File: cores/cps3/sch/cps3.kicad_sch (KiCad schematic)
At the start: 11 parts, among them CN6 Conn_02x27_Odd_Even, Q15 ZR

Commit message: additional_informaion_clk
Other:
- note added: "4-Pin Power Connector and 50-pin SCSI Data Cable Connector"
- note added: "CDROM Drive is a CR504-KCM 4X SCSI drive manufactured By Panasonic / Matsushita"
- note added: "Security Cartridge Slot"
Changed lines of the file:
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@@
     (effects (font (size 1.27 1.27)) (justify left bottom))
+  )
+  (text " Security Cartridge Slot" (at 71.12 119.38 180)
+    (effects (font (size 1.27 1.27)) (justify right bottom))
   )
   (text "This pin is connected to \npin 2 of CR7 (R0)\n\n" (at 36.83 72.39 90)
@@
     (effects (font (size 1.27 1.27)) (justify left bottom))
   )
+  (text "4-Pin Power Connector \nand 50-pin SCSI Data\nCable Connector"
+    (at 193.04 90.17 0)
+    (effects (font (size 1.27 1.27)) (justify left bottom))
+  )
   (text "P4" (at 185.42 88.9 0)
     (effects (font (size 1.27 1.27)) (justify left bottom))
@@
     (effects (font (size 1.27 1.27)) (justify left bottom))
   )
+  (text "CDROM Drive is a CR504-KCM 4X SCSI\ndrive manufactured By Panasonic \n/ Matsushita"
+    (at 193.04 96.52 0)
+    (effects (font (size 1.27 1.27)) (justify left bottom))
+  )

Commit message: wip_gll2
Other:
- sheet objects ports: added 2GLL2PPU[6..0], ~{RESET[0..3]}; removed 2GLL2PPU0, 2GLL_A[5..0], ~{RESET[4..1]}
- sheet ppu ports: added 2GLL2PPU[6..0]; removed 2GLL2PPU0, 2GLL_A[5..0]
- sheet simms_flash ports: added ~{RESET[0..3]}; removed ~{RESET[4..1]}
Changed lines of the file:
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@@
     (stroke (width 0) (type default) (color 0 0 0 0))
   )
-  (wire (pts (xy 194.31 162.56) (xy 212.09 162.56))
-    (stroke (width 0) (type default) (color 0 0 0 0))
-  )
   (bus (pts (xy 85.09 161.29) (xy 85.09 163.83))
     (stroke (width 0) (type default) (color 0 0 0 0))
@@
     (stroke (width 0) (type default) (color 0 0 0 0))
   )
-  (wire (pts (xy 223.52 26.67) (xy 240.03 26.67))
-    (stroke (width 0) (type default) (color 0 0 0 0))
-  )
   (bus (pts (xy 46.99 158.75) (xy 46.99 156.21))
     (stroke (width 0) (type default) (color 0 0 0 0))
@@
     (effects (font (size 1.27 1.27)) (justify left bottom))
   )
-  (label "2GLL_A[5..0]" (at 295.91 31.75 180)
+  (label "2GLL2PPU[6..0]" (at 295.91 31.75 180)
     (effects (font (size 1.27 1.27)) (justify right bottom))
   )
@@
     (effects (font (size 1.27 1.27)) (justify right bottom))
   )
-  (label "2GLL_A[5..0]" (at 212.09 119.38 180)
+  (label "2GLL2PPU[6..0]" (at 212.09 119.38 180)
     (effects (font (size 1.27 1.27)) (justify right bottom))
   )
@@
     (effects (font (size 1.27 1.27)) (justify left bottom))
   )
-  (label "~{RESET[4..1]}" (at 295.91 34.29 180)
+  (label "~{RESET[0..3]}" (at 295.91 34.29 180)
     (effects (font (size 1.27 1.27)) (justify right bottom))
   )
@@
     (effects (font (size 1.27 1.27)) (justify left bottom))
   )
-  (label "2GLL2PPU0" (at 223.52 26.67 0)
-    (effects (font (size 1.27 1.27)) (justify left bottom))
-  )
   (label "MAIN_A[28..0]" (at 295.91 152.4 180)
     (effects (font (size 1.27 1.27)) (justify right bottom))
@@
     (effects (font (size 1.27 1.27)) (justify left bottom))
   )
-  (label "2GLL2PPU0" (at 212.09 162.56 180)
-    (effects (font (size 1.27 1.27)) (justify right bottom))
-  )
   (label "VCC" (at 77.47 130.81 180)
     (effects (font (size 1.27 1.27)) (justify right bottom))
@@
     (effects (font (size 1.27 1.27)) (justify right bottom))
   )
-  (label "~{RESET[4..1]}" (at 138.43 259.08 0)
+  (label "~{RESET[0..3]}" (at 138.43 259.08 0)
     (effects (font (size 1.27 1.27)) (justify left bottom))
   )
@@
       (effects (font (size 1.27 1.27)) (justify left))
     )
-    (pin "~{RESET[4..1]}" input (at 156.21 259.08 180)
+    (pin "~{RESET[0..3]}" input (at 156.21 259.08 180)
       (effects (font (size 1.27 1.27)) (justify left))
     )
@@
       (effects (font (size 1.27 1.27)) (justify right))
     )
-    (pin "2GLL_A[5..0]" bidirectional (at 278.13 31.75 0)
+    (pin "2GLL2PPU[6..0]" bidirectional (at 278.13 31.75 0)
       (effects (font (size 1.27 1.27)) (justify right))
     )
@@
       (effects (font (size 1.27 1.27)) (justify right))
     )
-    (pin "~{RESET[4..1]}" output (at 278.13 34.29 0)
+    (pin "~{RESET[0..3]}" output (at 278.13 34.29 0)
       (effects (font (size 1.27 1.27)) (justify right))
     )
@@
       (effects (font (size 1.27 1.27)) (justify left))
     )
-    (pin "2GLL2PPU0" bidirectional (at 240.03 26.67 180)
-      (effects (font (size 1.27 1.27)) (justify left))
-    )
     (pin "2GLL2CCU0" bidirectional (at 240.03 29.21 180)
       (effects (font (size 1.27 1.27)) (justify left))
@@
       (effects (font (size 1.27 1.27)) (justify right))
     )
-    (pin "2GLL_A[5..0]" bidirectional (at 194.31 119.38 0)
+    (pin "2GLL2PPU[6..0]" bidirectional (at 194.31 119.38 0)
       (effects (font (size 1.27 1.27)) (justify right))
     )
@@
       (effects (font (size 1.27 1.27)) (justify right))
     )
-    (pin "2GLL2PPU0" bidirectional (at 194.31 162.56 0)
-      (effects (font (size 1.27 1.27)) (justify right))
-    )

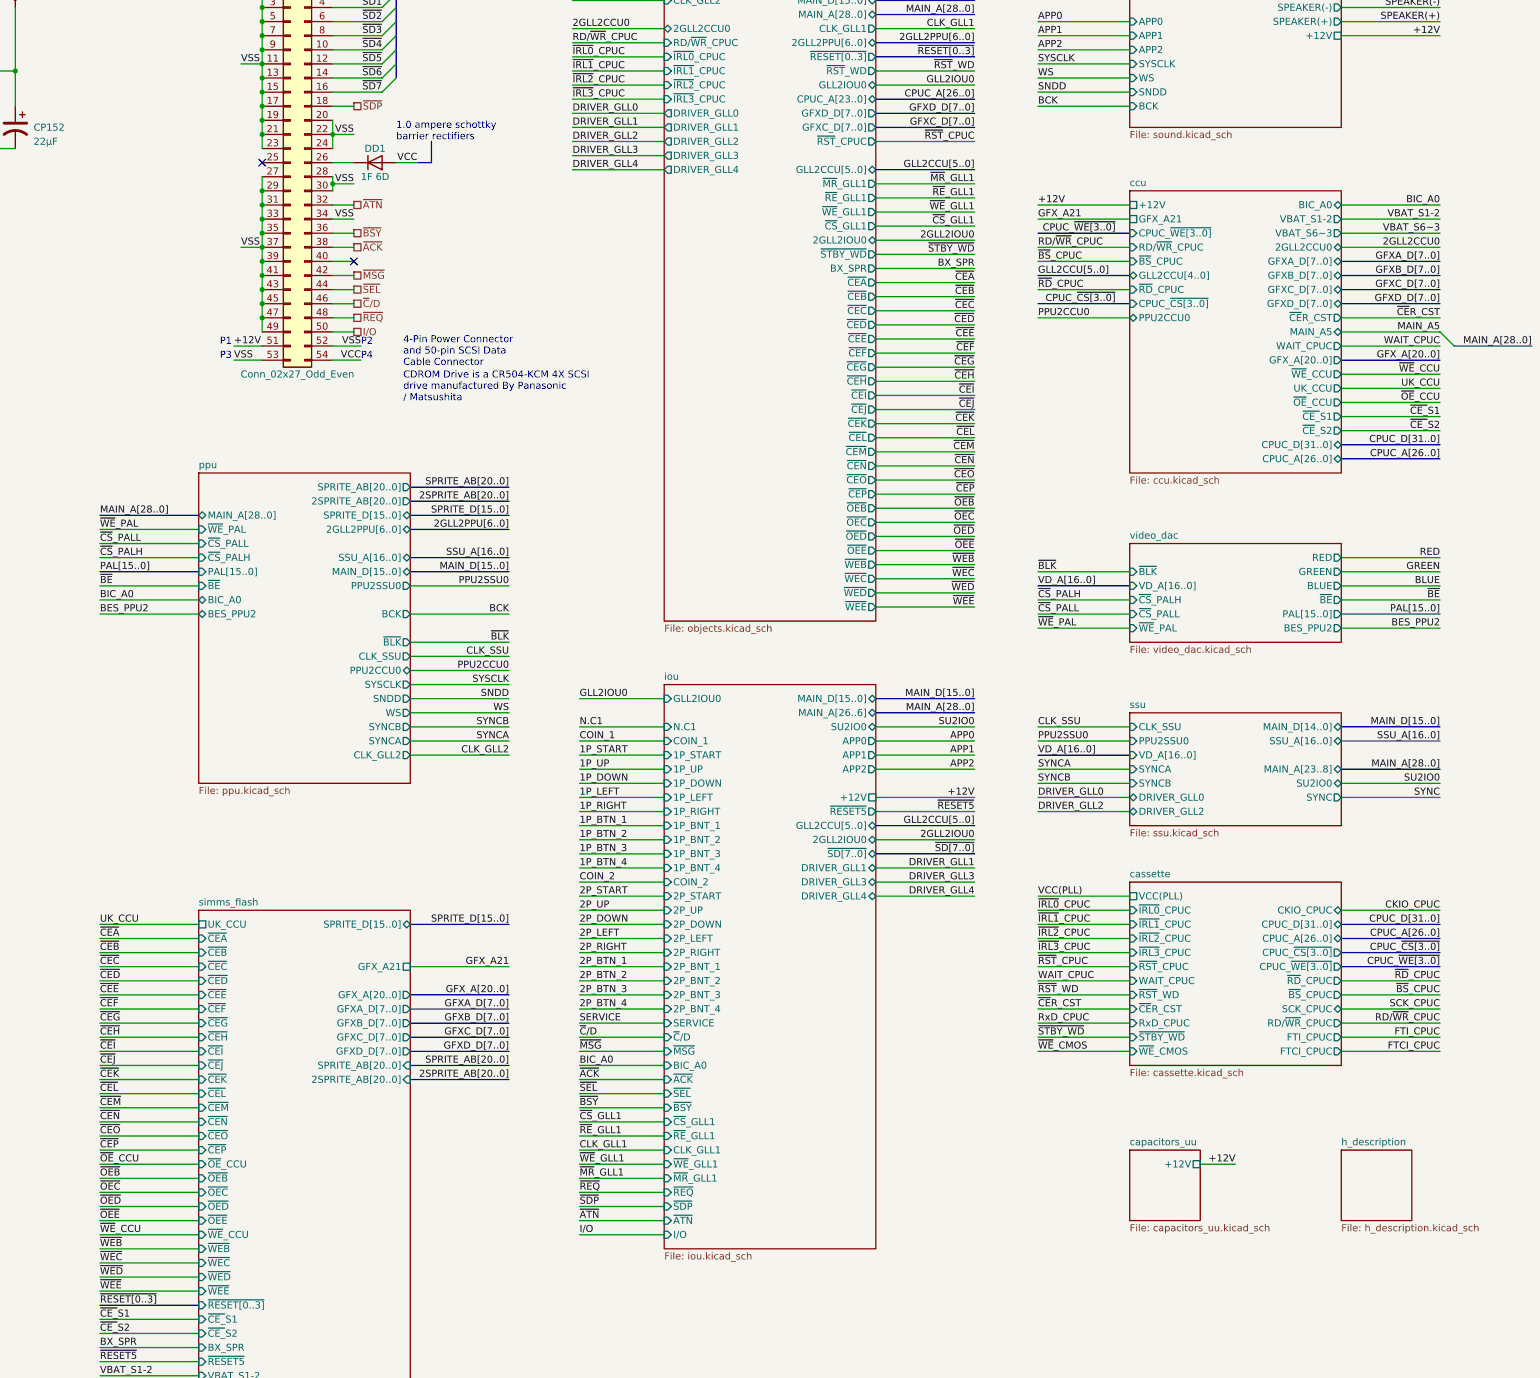
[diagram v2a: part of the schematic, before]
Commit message: cps3 wrong signal names #254
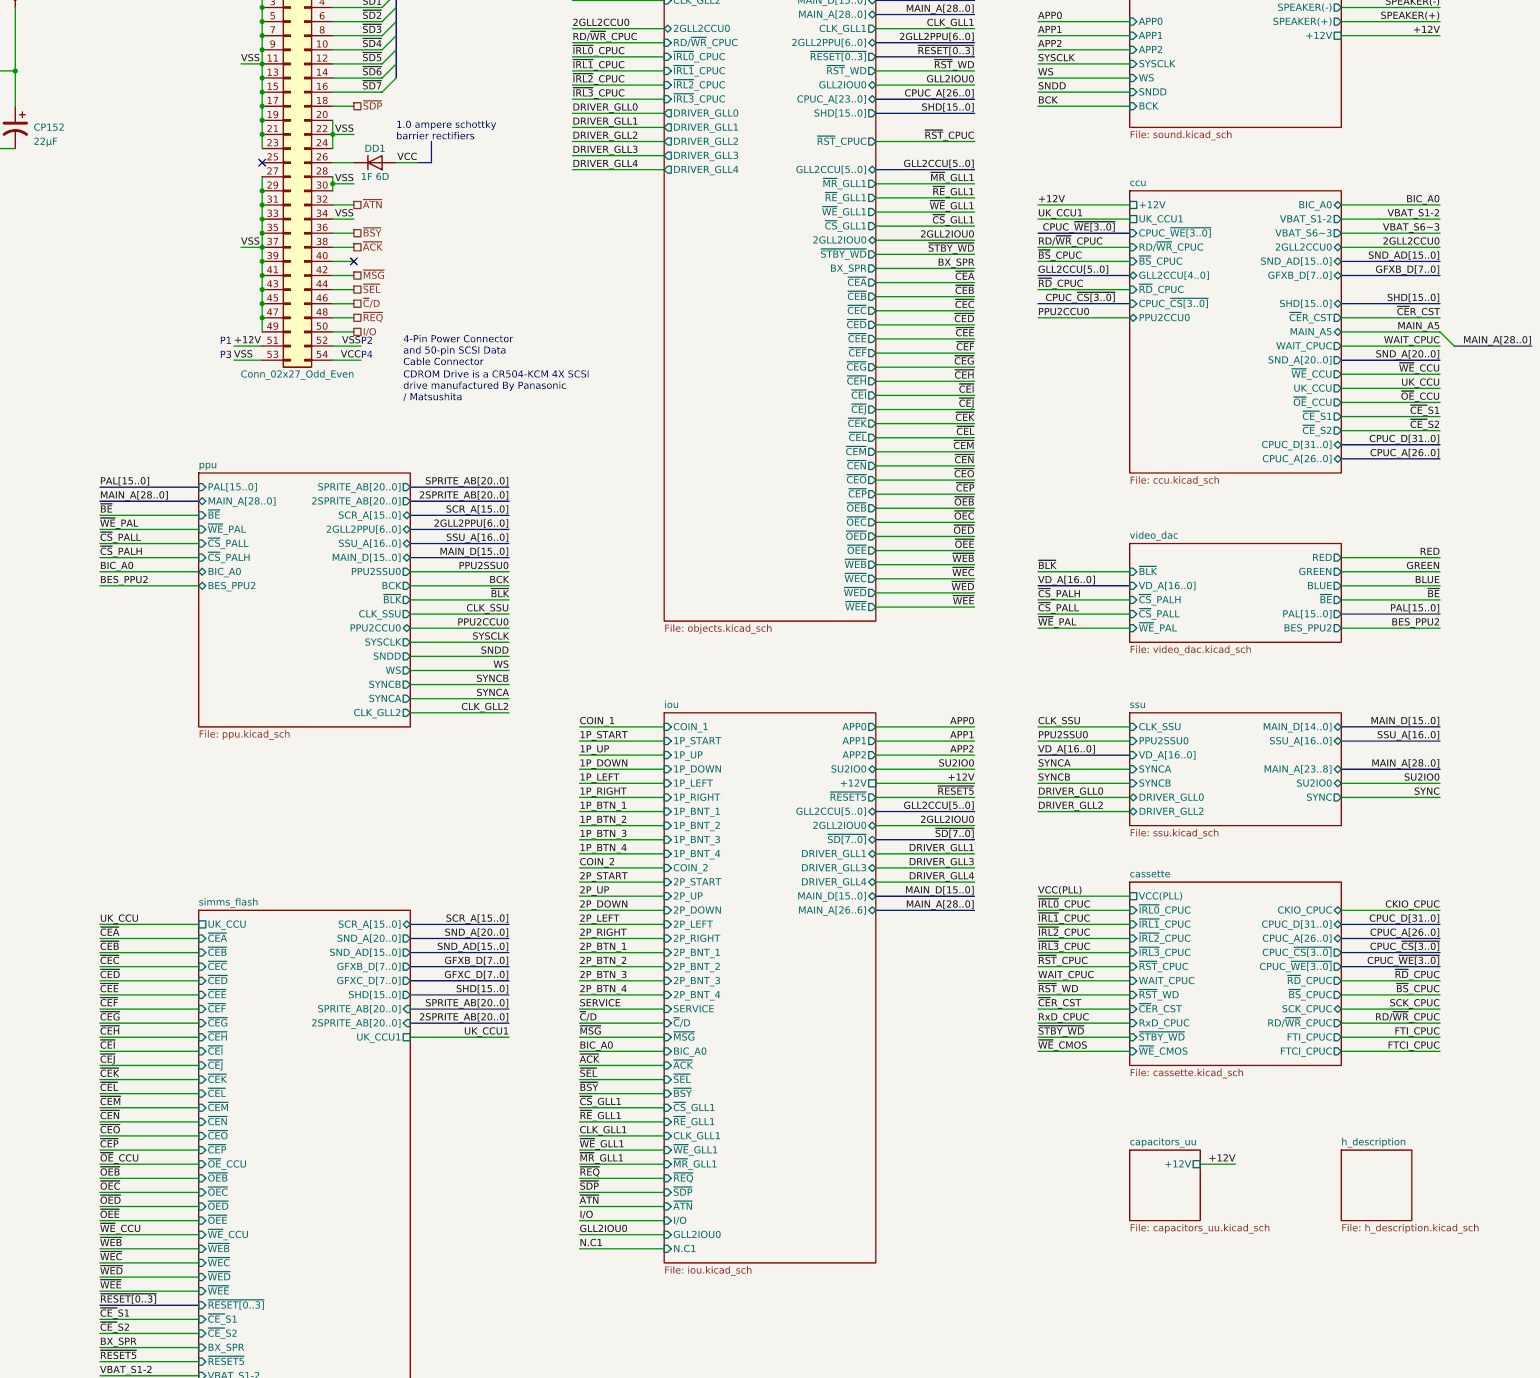
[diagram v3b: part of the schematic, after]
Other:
- sheet ccu ports: added SHD[15..0], SND_AD[15..0], SND_A[20..0], UK_CCU1; removed GFXA_D[7..0], GFXC_D[7..0], GFXD_D[7..0], GFX_A21, GFX_A[20..0]
- sheet objects ports: added SHD[15..0]; removed GFXC_D[7..0], GFXD_D[7..0]
- sheet ppu ports: added SCR_A[15..0]; removed SPRITE_D[15..0]
- sheet simms_flash ports: added SCR_A[15..0], SHD[15..0], SND_AD[15..0], SND_A[20..0], UK_CCU1; removed GFXA_D[7..0], GFXD_D[7..0], GFX_A21, GFX_A[20..0], SPRITE_D[15..0]

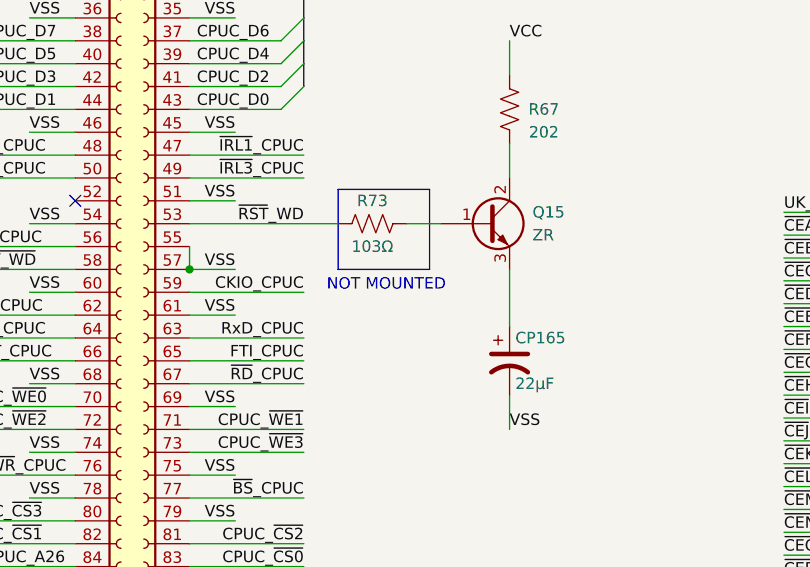
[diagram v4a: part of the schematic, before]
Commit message: sch: not mounted -> not populated
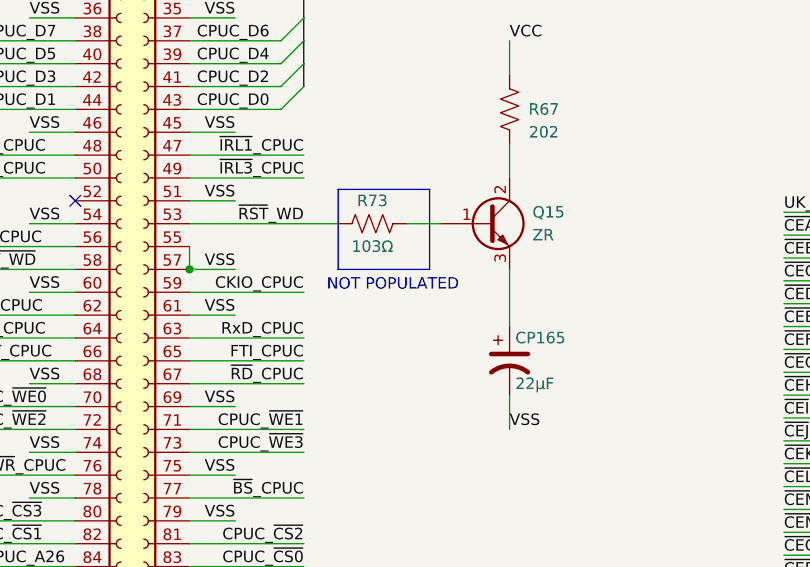
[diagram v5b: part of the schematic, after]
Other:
- note added: "NOT POPULATED"
- note removed: "NOT MOUNTED"
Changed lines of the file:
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@@
     (effects (font (size 1.27 1.27)) (justify left bottom))
   )
-  (text "NOT MOUNTED" (at 87.63 199.39 0)
+  (text "NOT POPULATED" (at 87.63 199.39 0)
     (effects (font (size 1.27 1.27)) (justify left bottom))
   )
